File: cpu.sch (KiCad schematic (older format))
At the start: 5 parts, among them U15 Z80CPU, U16 GAL16V8, U17 GAL16V8

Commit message: Added RTC
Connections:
- net ~RTCS: now reaches U16.15 (IO5)
- no-connect marks 16 -> 15
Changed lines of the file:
@@
 Wire Wire Line
 	8850 4000 8950 4000
-NoConn ~ 8850 4100
 Wire Wire Line
 	7850 4100 7700 4100
@@
 	1    0    0    -1
 $EndComp
+Text GLabel 9200 4100 2    50   Output ~ 0
+~RTCS
+Wire Wire Line
+	9200 4100 8850 4100
 Wire Bus Line
 	4650 3200 4650 3950

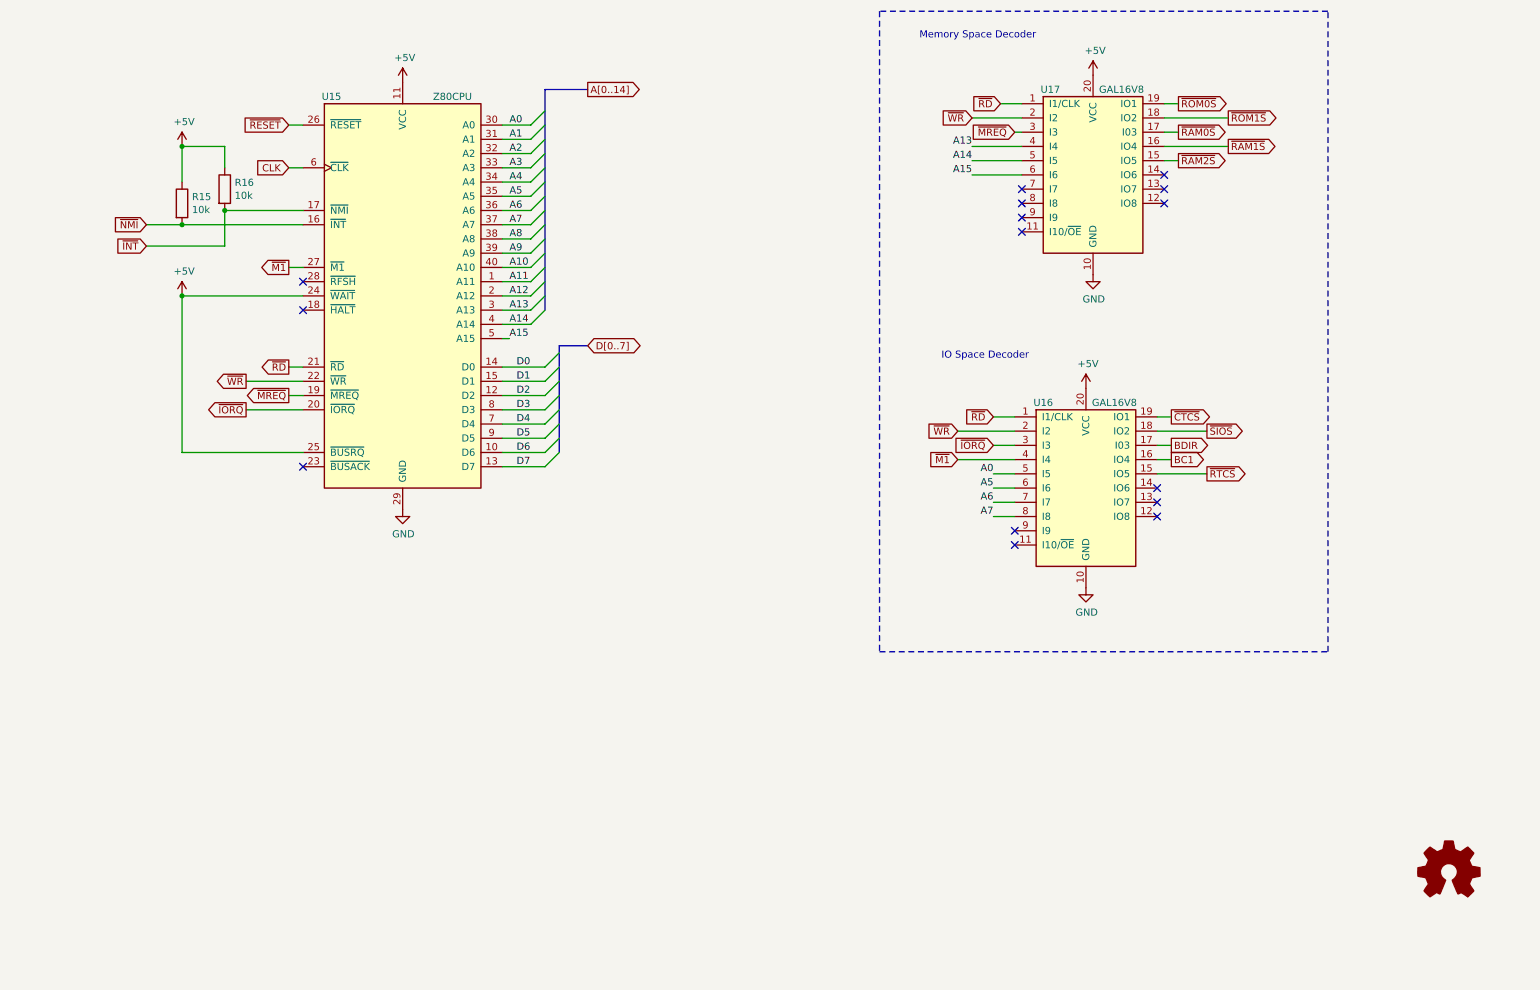
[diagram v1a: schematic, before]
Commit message: Added PIO to schematic
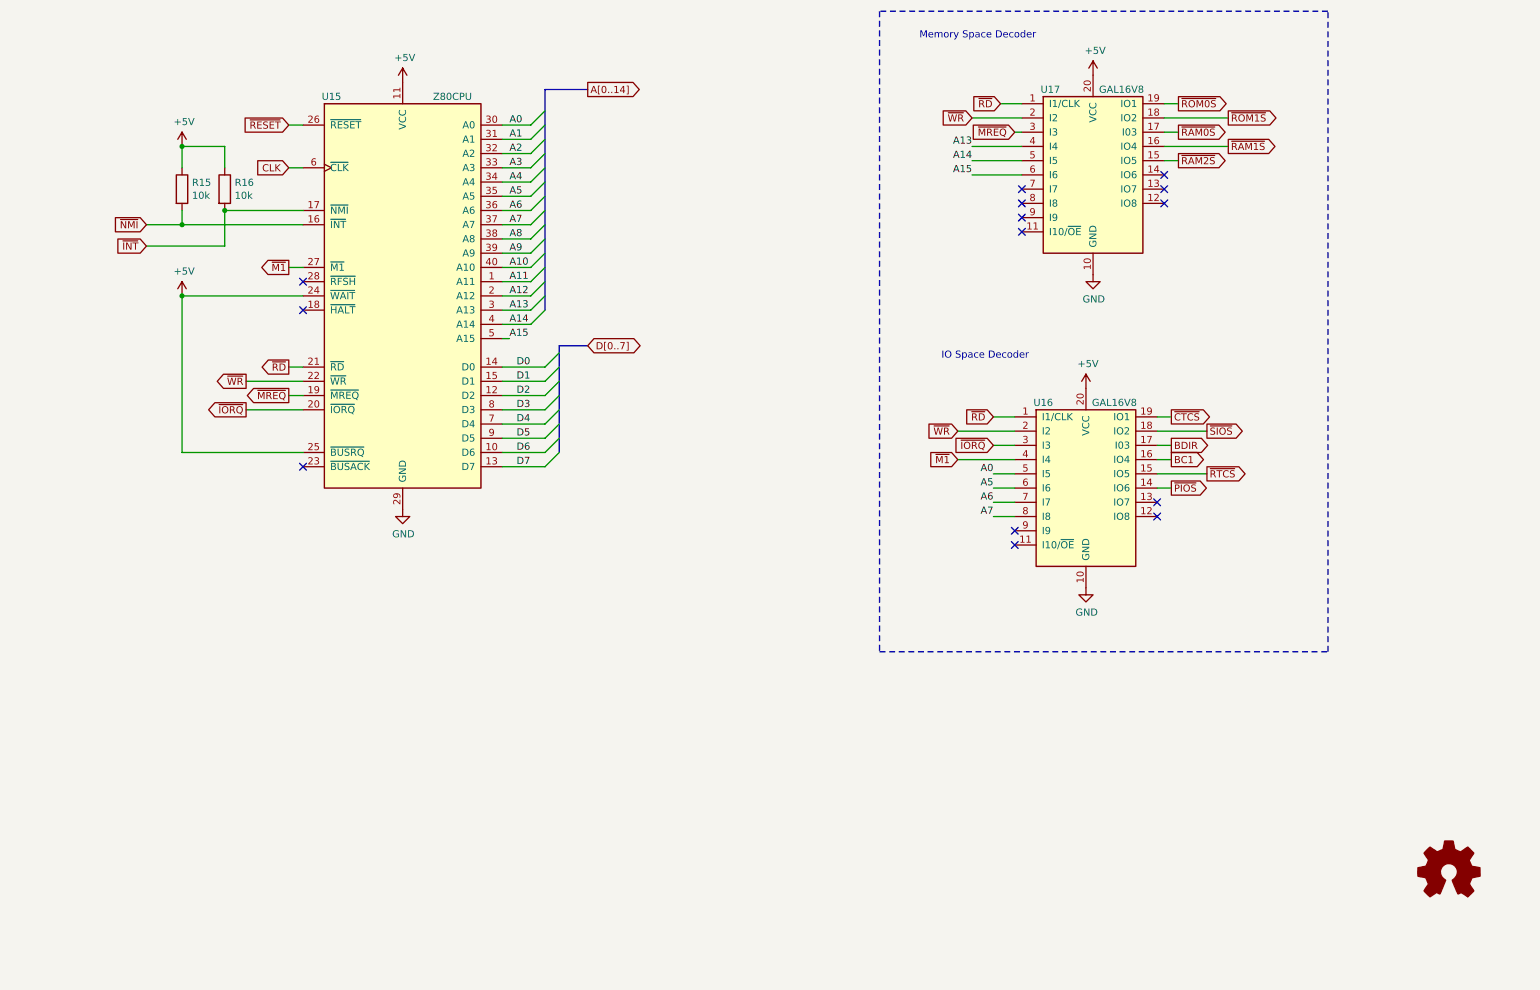
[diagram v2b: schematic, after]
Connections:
- net ~PIOS: now reaches U16.14 (IO6)
- no-connect marks 15 -> 14
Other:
- moved on the sheet: R15
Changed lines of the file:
@@
 L Device:R R?
 U 1 1 608E47E0
-P 2000 2200
+P 2000 2100
 AR Path="/608E47E0" Ref="R?"  Part="1"
 AR Path="/608D2E51/608E47E0" Ref="R15"  Part="1"
-F 0 "R15" H 2070 2246 50  0000 L CNN
-F 1 "10k" H 2070 2155 50  0000 L CNN
-F 2 "" V 1930 2200 50  0001 C CNN
-F 3 "~" H 2000 2200 50  0001 C CNN
-	1    2000 2200
-	1    0    0    -1
-$EndComp
-Wire Wire Line
-	2850 2350 2000 2350
+F 0 "R15" H 2070 2146 50  0000 L CNN
+F 1 "10k" H 2070 2055 50  0000 L CNN
+F 2 "" V 1930 2100 50  0001 C CNN
+F 3 "~" H 2000 2100 50  0001 C CNN
+	1    2000 2100
+	1    0    0    -1
+$EndComp
 Wire Wire Line
 	2850 2250 2300 2250
 Connection ~ 2000 2850
 Wire Wire Line
-	2000 2050 2000 1800
+	2000 1950 2000 1800
 Wire Wire Line
 	2300 1950 2300 1800
@@
 $EndComp
 Connection ~ 2000 1800
-Wire Wire Line
-	2000 2350 1750 2350
-Connection ~ 2000 2350
 Wire Wire Line
 	2300 2250 2300 2500
@@
 	1    0    0    -1
 $EndComp
-NoConn ~ 8850 4200
 NoConn ~ 8850 4300
 NoConn ~ 8850 4400
@@
 Wire Wire Line
 	9200 4100 8850 4100
+Text GLabel 8950 4200 2    50   Output ~ 0
+~PIOS
+Wire Wire Line
+	8850 4200 8950 4200
+Wire Wire Line
+	1750 2350 2000 2350
+Wire Wire Line
+	2000 2250 2000 2350
 Wire Bus Line
 	4650 3200 4650 3950
 Wire Bus Line
 	4550 1400 4550 2950
+Connection ~ 2000 2350
+Wire Wire Line
+	2000 2350 2850 2350
 $EndSCHEMATC

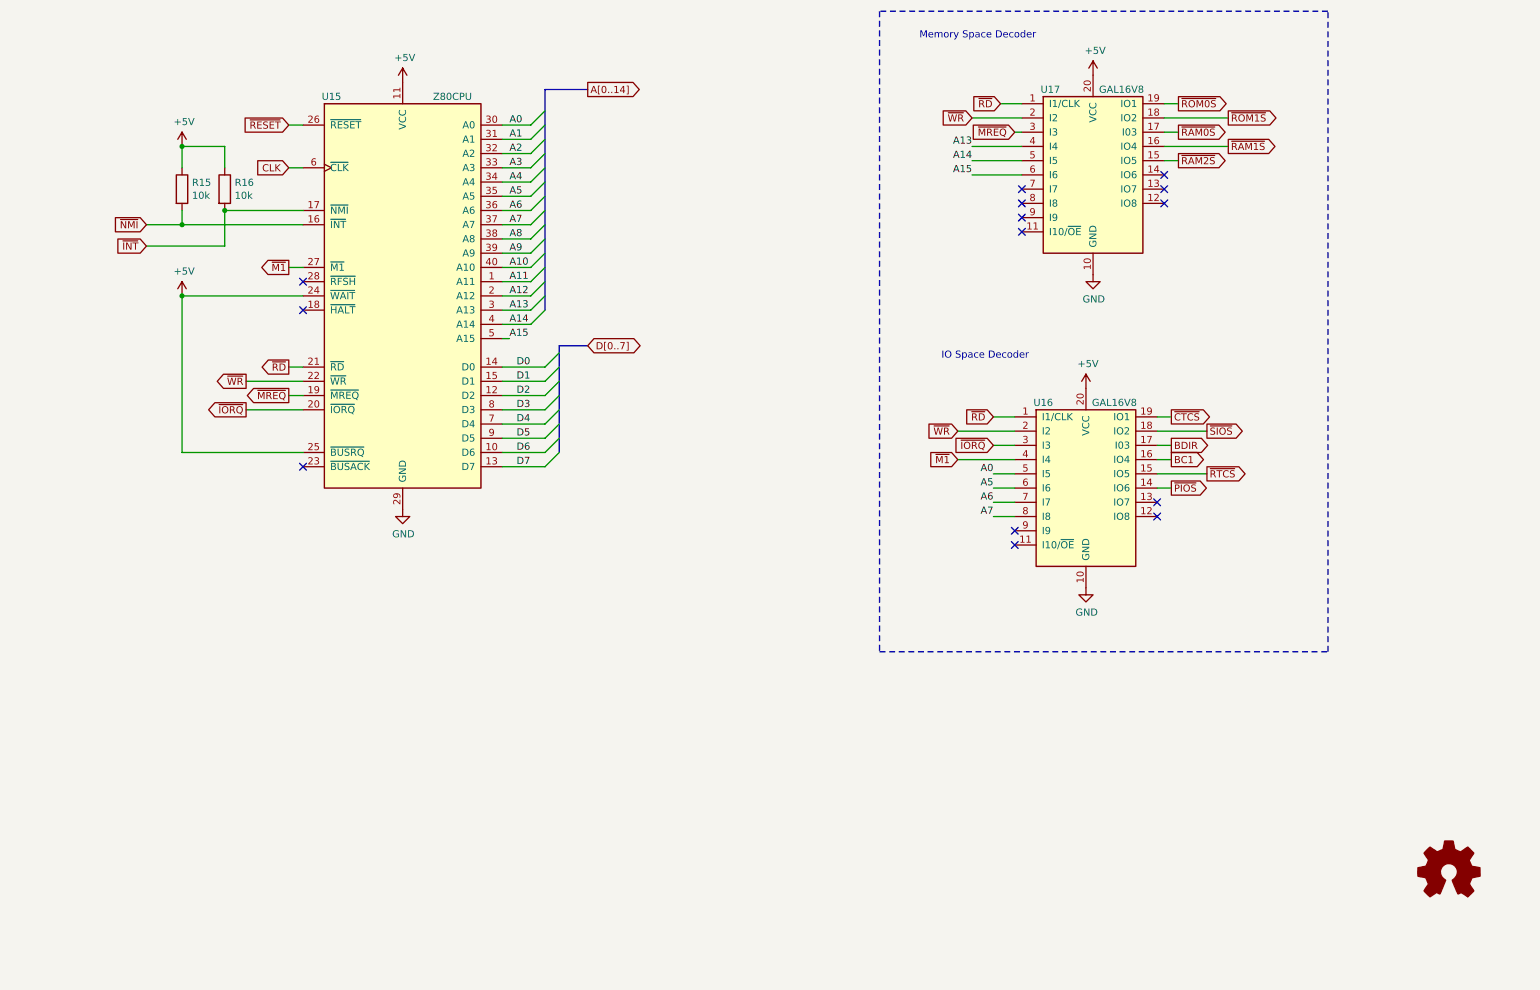
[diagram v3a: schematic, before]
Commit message: Added expansion bus and GPIO ports
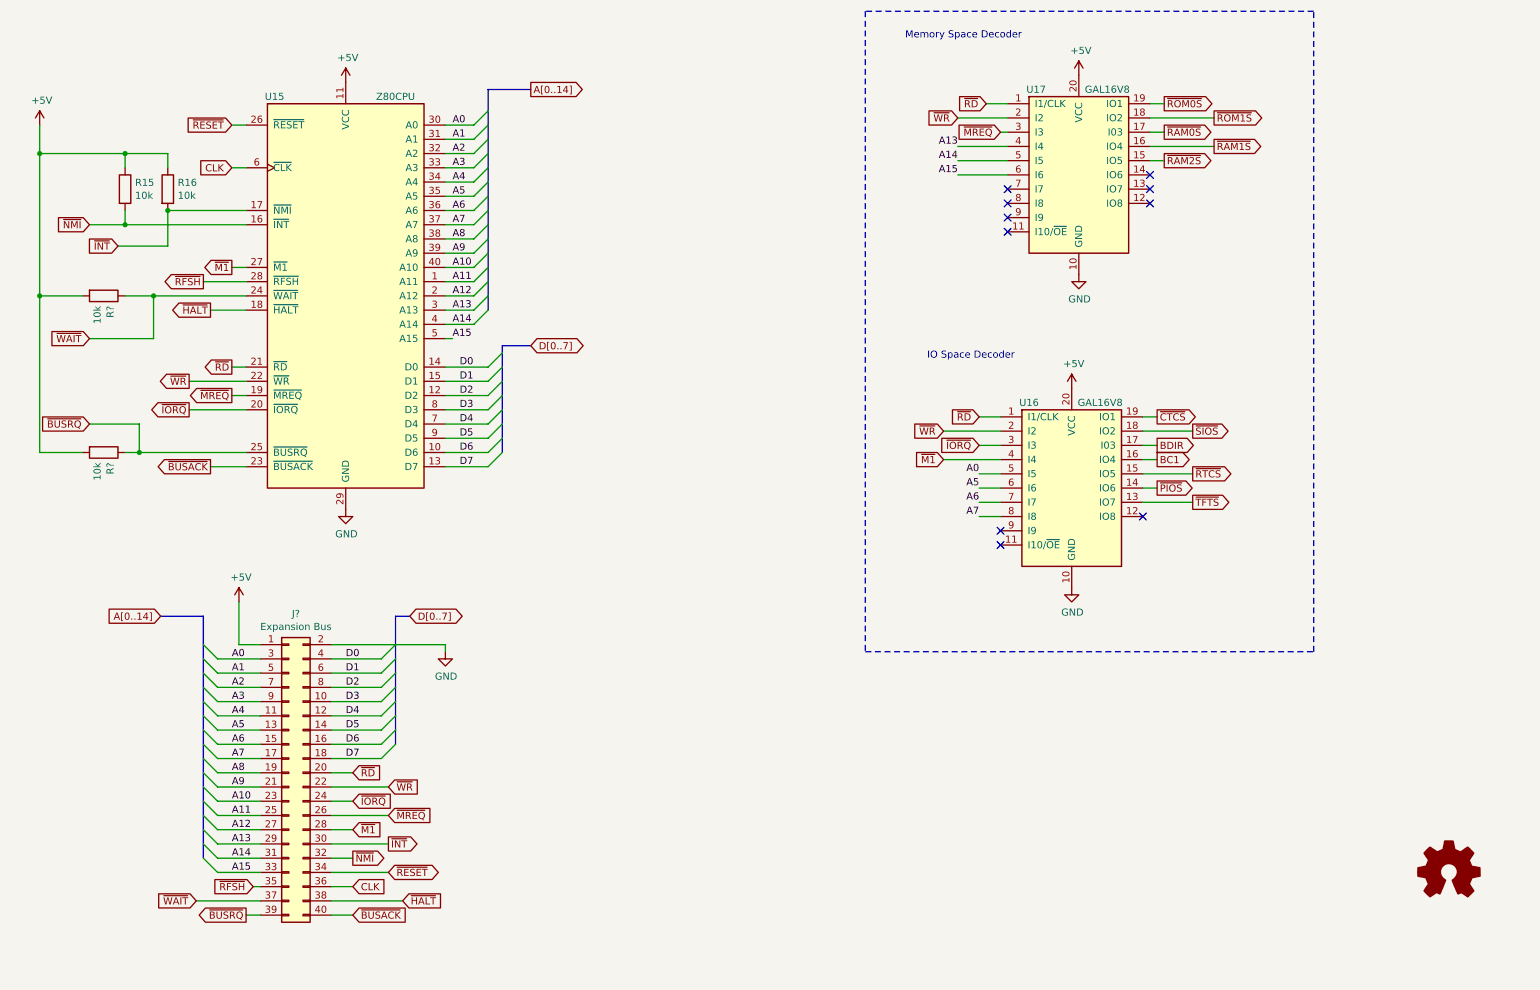
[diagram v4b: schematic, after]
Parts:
- added J?: Expansion Bus, symbol Connector_Generic:Conn_02x20_Odd_Even
- added R? (x2): 10k, symbol Device:R
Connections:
- net +5V: now also J?.1 (Pin_1), R?.2, R?.2; no longer U15.24 (~WAIT~), U15.25 (~BUSRQ~)
- net A0: now also J?.3 (Pin_3)
- net A1: now also J?.5 (Pin_5)
- net A10: now also J?.23 (Pin_23)
- net A11: now also J?.25 (Pin_25)
- net A12: now also J?.27 (Pin_27)
- net A13: now also J?.29 (Pin_29)
- net A14: now also J?.31 (Pin_31)
- net A15: now also J?.33 (Pin_33)
- net A2: now also J?.7 (Pin_7)
- net A3: now also J?.9 (Pin_9)
- net A4: now also J?.11 (Pin_11)
- net A5: now also J?.13 (Pin_13)
- net A6: now also J?.15 (Pin_15)
- net A7: now also J?.17 (Pin_17)
- net A8: now also J?.19 (Pin_19)
- net A9: now also J?.21 (Pin_21)
- net CLK: now also J?.36 (Pin_36)
- net D0: now also J?.4 (Pin_4)
- net D1: now also J?.6 (Pin_6)
- net D2: now also J?.8 (Pin_8)
- net D3: now also J?.10 (Pin_10)
- net D4: now also J?.12 (Pin_12)
- net D5: now also J?.14 (Pin_14)
- net D6: now also J?.16 (Pin_16)
- net D7: now also J?.18 (Pin_18)
- net GND: now also J?.2 (Pin_2)
- net ~INT: now also J?.30 (Pin_30)
- net ~IORQ: now also J?.24 (Pin_24)
- net ~M1: now also J?.28 (Pin_28)
- net ~MREQ: now also J?.26 (Pin_26)
- net ~NMI: now also J?.32 (Pin_32)
- net ~RD: now also J?.20 (Pin_20)
- net ~RESET: now also J?.34 (Pin_34)
- net ~WR: now also J?.22 (Pin_22)
- net ~HALT: now reaches U15.18 (~HALT~)
- net ~HALT: now also J?.38 (Pin_38)
- net ~BUSACK: now reaches U15.23 (~BUSACK~)
- net ~BUSACK: now also J?.40 (Pin_40)
- net ~RFSH: now reaches U15.28 (~RFSH~)
- net ~RFSH: now also J?.35 (Pin_35)
- net ~TFTS: now reaches U16.13 (IO7)
- new net ~BUSRQ: J?.39 (Pin_39), R?.1, U15.25 (~BUSRQ~)
- new net ~WAIT: J?.37 (Pin_37), R?.1, U15.24 (~WAIT~)
- no-connect marks 14 -> 10
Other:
- moved on the sheet: R15, R16, U15, U16, U17

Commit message: Updated schematic
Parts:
- added SW5: NMI, symbol Switch:SW_Push
- J11: renamed from J?; footprint (none) -> Connector_PinSocket_2.54mm:PinSocket_2x20_P2.54mm_Vertical
- R15, R16: footprint (none) -> Resistor_THT:R_Axial_DIN0207_L6.3mm_D2.5mm_P10.16mm_Horizontal
- R26, R27: renamed from R?; footprint (none) -> Resistor_THT:R_Axial_DIN0207_L6.3mm_D2.5mm_P10.16mm_Horizontal
- U15: footprint Package_DIP:DIP-40_W15.24mm_Socket -> Package_DIP:DIP-40_W15.24mm_Socket_LongPads
- U16, U17: footprint (none) -> Package_DIP:DIP-20_W7.62mm_Socket_LongPads
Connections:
- net GND: now also SW5.2
- net ~NMI: now also SW5.1
- net ~CFS: now reaches U16.12 (IO8)
- no-connect marks 10 -> 9
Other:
- note added: "CPU"
- note added: "Copyright © Jaap Geurts 2021\n\nThis documentation describes Open Hardware and is licensed under the CERN OHL v. 1.1.\nYou may redistribute and modify this documentation under the terms of the CERN OHL v.1.1.\n(http://ohwr.org/cernohl). This documentation is distributed WITHOUT ANY EXPRESS OR IMPLIED\nWARRANTY, INCLUDING OF MERCHANTABILITY, SATISFACTORY QUALITY AND FITNESS FOR A PARTICULAR PURPOS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"
- note added: "Expansion bus"
- moved on the sheet: J11

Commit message: All footprints assigned
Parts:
- SW5: footprint (none) -> Button_Switch_THT:SW_PUSH_6mm
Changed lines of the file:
@@
 L power:GND #PWR?
 U 1 1 60B4795F
-P 3800 5500
+P 3300 5050
 AR Path="/60B4795F" Ref="#PWR?"  Part="1"
 AR Path="/608D2E51/60B4795F" Ref="#PWR0128"  Part="1"
-F 0 "#PWR0128" H 3800 5250 50  0001 C CNN
-F 1 "GND" H 3805 5327 50  0000 C CNN
-F 2 "" H 3800 5500 50  0001 C CNN
-F 3 "" H 3800 5500 50  0001 C CNN
-	1    3800 5500
+F 0 "#PWR0128" H 3300 4800 50  0001 C CNN
+F 1 "GND" H 3305 4877 50  0000 C CNN
+F 2 "" H 3300 5050 50  0001 C CNN
+F 3 "" H 3300 5050 50  0001 C CNN
+	1    3300 5050
 	1    0    0    -1
 $EndComp
 Wire Wire Line
-	3800 5500 3800 5450
+	3300 5050 3300 5000
 $Comp
 L power:+5V #PWR?
@@
 F 0 "SW5" H 5150 4585 50  0000 C CNN
 F 1 "NMI" H 5150 4494 50  0000 C CNN
-F 2 "" H 5150 4500 50  0001 C CNN
+F 2 "Button_Switch_THT:SW_PUSH_6mm" H 5150 4500 50  0001 C CNN
 F 3 "~" H 5150 4500 50  0001 C CNN
 	1    5150 4300
@@
 Wire Notes Line
 	5500 900  850  900
+Text Notes 1000 1050 0    47   ~ 0
+CPU
 Wire Wire Line
-	3000 5450 3800 5450
+	3000 5450 3100 5450
+Wire Wire Line
+	3100 5450 3100 5000
+Wire Wire Line
+	3100 5000 3300 5000
 Wire Bus Line
 	3450 5250 3450 6150
@@
 Wire Bus Line
 	2100 5250 2100 6950
-Text Notes 1000 1050 0    47   ~ 0
-CPU
 $EndSCHEMATC

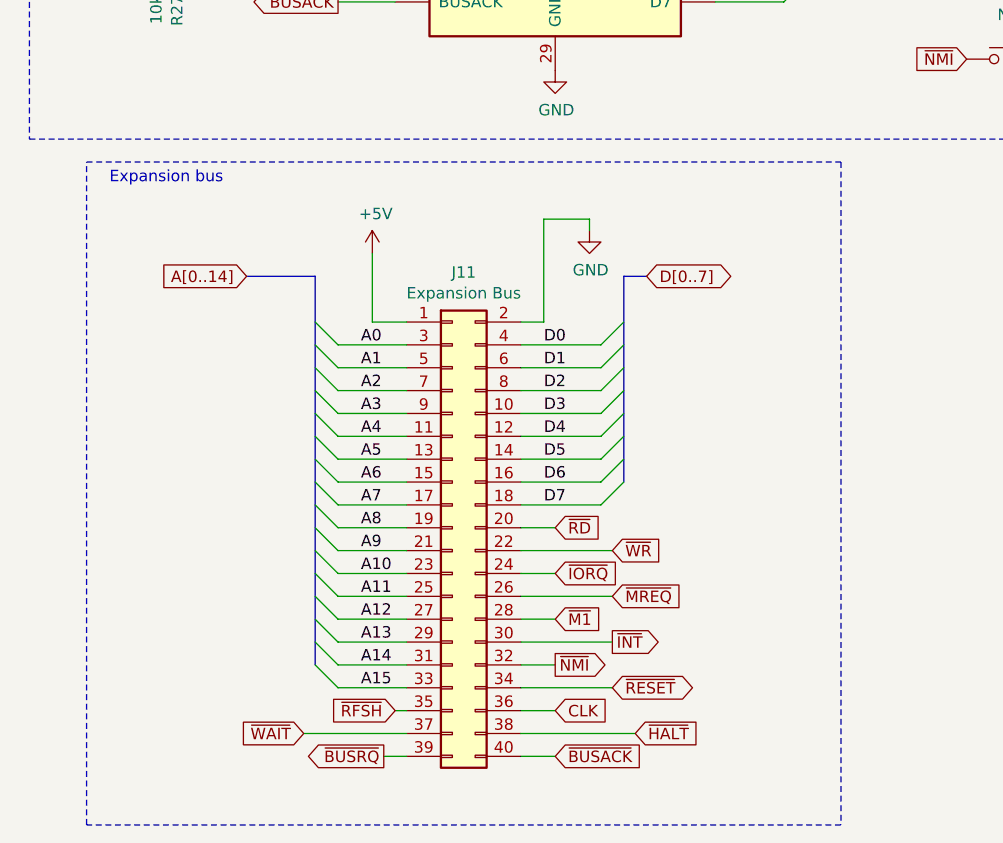
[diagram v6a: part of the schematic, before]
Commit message: PCB tracing done
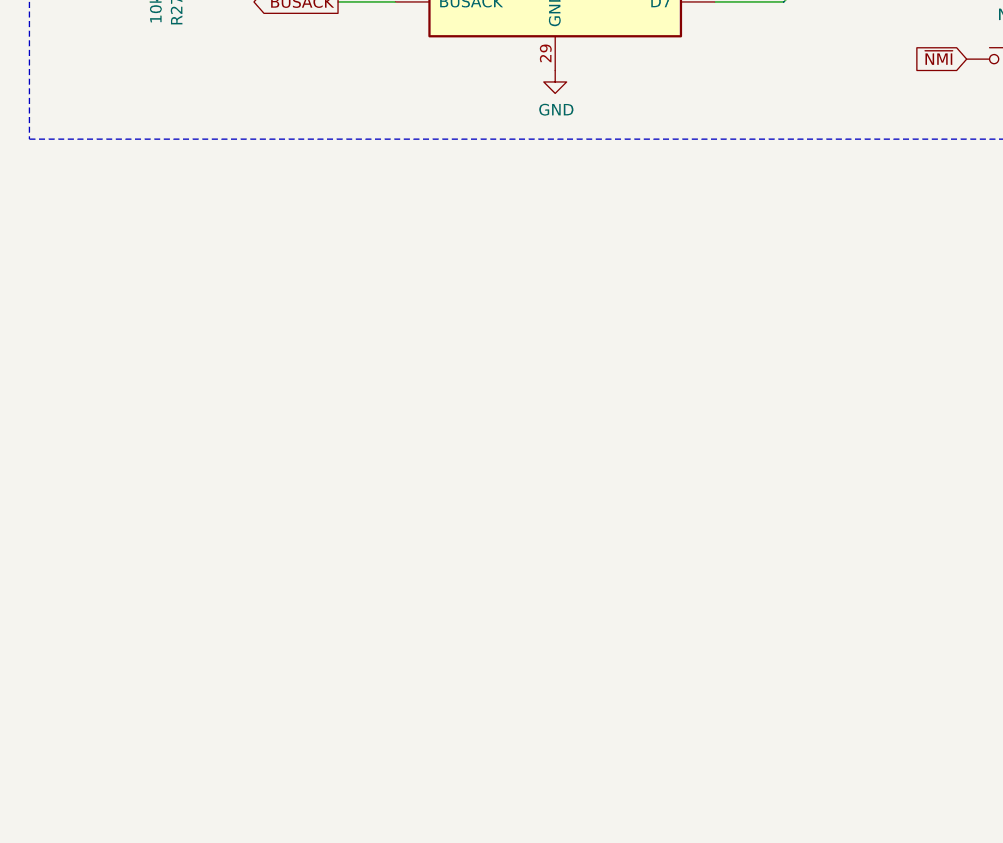
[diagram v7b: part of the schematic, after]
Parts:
- removed J11: Expansion Bus, Connector_PinSocket_2.54mm:PinSocket_2x20_P2.54mm_Vertical, symbol Connector_Generic:Conn_02x20_Odd_Even
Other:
- note removed: "Expansion bus"
